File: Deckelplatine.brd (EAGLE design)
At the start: 110 x 75 mm, 61 parts, among them IC1 MAX1487EESA+, IC2 74HCT595D, IC3 74HCT595D, IC4 74HCT595D, IC5 74HCT595D, IC6 74HCT595D, J1 52808-2570, U1 LM2676S, X1 236-406/000-023, X2 233-502

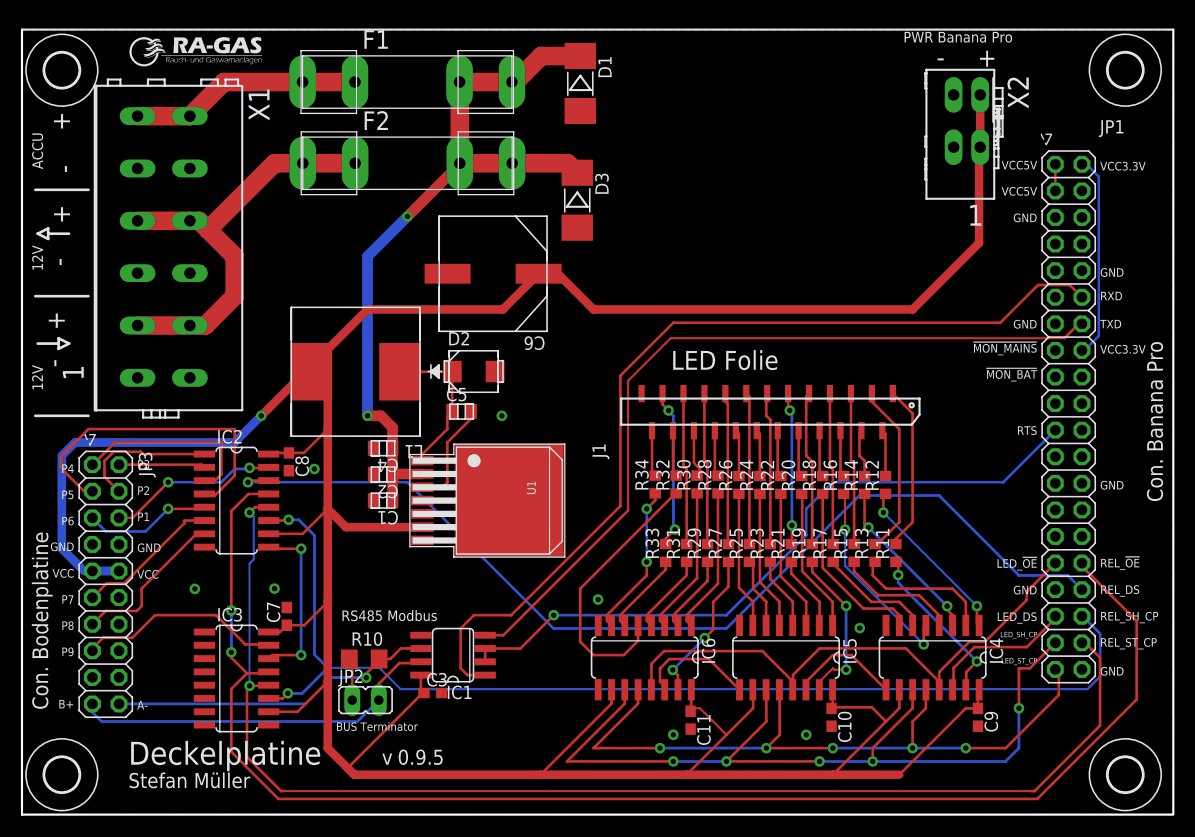
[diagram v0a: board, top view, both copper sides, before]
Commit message: Ein wenig Kosmetik auf der Deckelplatine
Beschriftungen angepasst
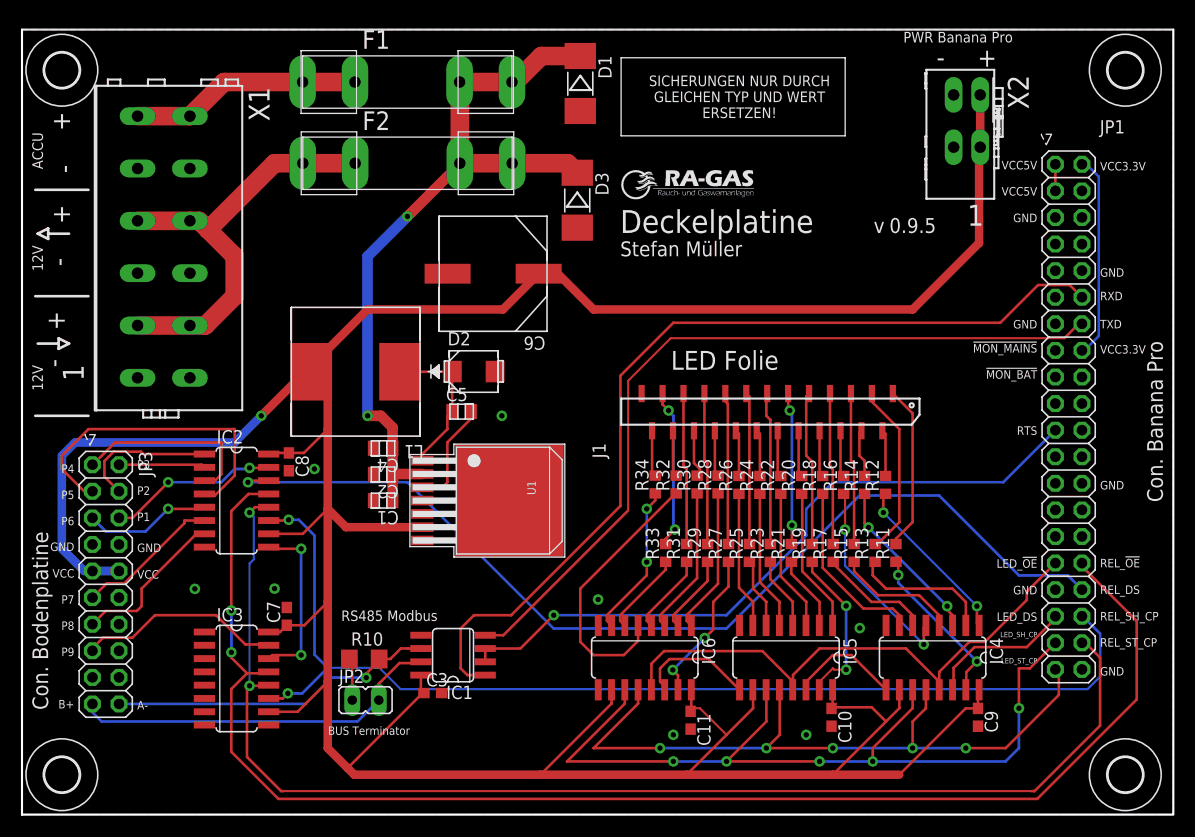
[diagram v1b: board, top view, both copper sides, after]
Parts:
- added U$4: (no value), xMZ-Mod-Touch-Bodenplatine:TEXT_FUSE-SMALL
- F1: value 0.63AT -> 2AT
- moved U$3 69.2 mm to (57.1, 53.3)
- moved U$2 48.7 mm to (57.3, 58.8)
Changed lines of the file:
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@@
 <layer number="47" name="Measures" color="7" fill="1" visible="no" active="yes"/>
 <layer number="48" name="Document" color="7" fill="1" visible="no" active="yes"/>
-<layer number="49" name="Reference" color="7" fill="1" visible="no" active="yes"/>
+<layer number="49" name="Reference" color="7" fill="1" visible="yes" active="yes"/>
 <layer number="50" name="dxf" color="7" fill="1" visible="no" active="no"/>
 <layer number="51" name="tDocu" color="6" fill="1" visible="yes" active="yes"/>
@@
 <text x="109" y="29.85" size="1.5" layer="21" font="vector" ratio="10" rot="R90">Con. Banana Pro</text>
 <text x="30.5" y="18.5" size="1" layer="21" font="vector" ratio="15">RS485 Modbus</text>
-<text x="30" y="8" size="0.8" layer="21" font="vector" ratio="10">BUS Terminator</text>
+<text x="29.238" y="7.619" size="0.8" layer="21" font="vector" ratio="10">BUS Terminator</text>
 <text x="84.2018" y="73.77" size="1.016" layer="21" font="vector" ratio="10">PWR Banana Pro</text>
 <text x="91.29" y="71.45" size="1.778" layer="21" font="vector" ratio="15">+</text>
@@
 <attribute name="OC_FARNELL" value="1283529" x="14" y="54.08" size="1.778" layer="27" rot="R180" display="off"/>
 <attribute name="NAME" x="21.655" y="69.5127" size="2" layer="25" font="vector" ratio="10" rot="R270"/>
-<attribute name="VALUE" x="21.65" y="49.1927" size="2" layer="27" font="vector" ratio="10" rot="R270"/>
+<attribute name="VALUE" x="21.65" y="68.2427" size="2" layer="27" font="vector" ratio="10" rot="R270"/>
 </element>
 <element name="X2" library="con-wago_233" package="P-233-502" value="233-502" x="90" y="65" rot="R270">
@@
 <attribute name="MPN" value="" x="105.41" y="3.81" size="1.778" layer="27" display="off"/>
 </element>
-<element name="F1" library="fuse-littlefuse" package="01110005MR" value="0.63AT" x="36.8092" y="69.99">
+<element name="F1" library="fuse-littlefuse" package="01110005MR" value="2AT" x="36.8092" y="69.99">
 <attribute name="OC_FARNELL" value="1155771" x="36.8092" y="69.99" size="1.778" layer="27" display="off"/>
 <attribute name="OC_FARNELL_ALTERNATIVE" value="01110005MR" x="36.8092" y="69.99" size="1.778" layer="27" display="off"/>
@@
 <attribute name="MPN" value="01110005MR" x="36.8092" y="69.99" size="1.778" layer="27" display="off"/>
 </element>
-<element name="U$2" library="xMZ-Mod-Touch-Bodenplatine" package="LOGO_RA-GAS-SMALL" value="" x="10.27" y="71.5"/>
-<element name="U$3" library="xMZ-Mod-Touch-Bodenplatine" package="TEXT_NAME_VERSION_AUTHOR-SMALL" value="" x="10.16" y="2.54"/>
+<element name="U$2" library="xMZ-Mod-Touch-Bodenplatine" package="LOGO_RA-GAS-SMALL" value="" x="57.26" y="58.8"/>
+<element name="U$3" library="xMZ-Mod-Touch-Bodenplatine" package="TEXT_NAME_VERSION_AUTHOR-SMALL" value="" x="57.15" y="53.34"/>
 <element name="F2" library="fuse-littlefuse" package="01110005MR" value="2AT" x="36.83" y="62.23">
 <attribute name="OC_FARNELL_ALTERNATIVE" value="01110005MR" x="36.83" y="62.23" size="1.778" layer="27" font="vector" ratio="15" display="off"/>
@@
 <attribute name="OC_FARNELL" value="1625106" x="53.34" y="69.85" size="1.778" layer="27" font="vector" ratio="15" rot="R270" display="off"/>
 </element>
+<element name="U$4" library="xMZ-Mod-Touch-Bodenplatine" package="TEXT_FUSE-SMALL" value="" x="68.58" y="68.58"/>
 </elements>
 <signals>
@@
 </board>
 </drawing>
+<compatibility>
+<note version="6.3" minversion="6.2.2" severity="warning">
+Since Version 6.2.2 text objects can contain more than one line,
+which will not be processed correctly with this version.
+</note>
+</compatibility>
 </eagle>
